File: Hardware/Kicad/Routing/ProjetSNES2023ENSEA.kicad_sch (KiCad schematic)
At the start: 43 parts, among them J1 Conn_01x07_Socket, Q1 2N7002, Q2 2N7002, Q3 2N7002, SW1 SW_Push, U1 NRF24L01, U2 AMS1117-3.3, U3 STM32L412KBTx, Y1 16 MHz

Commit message: Updated Schematic & PCB
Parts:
- renumbered D2 to D1, D1 to D2, R9 to R10, R10 to R9
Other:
- note added: "LEDs System"
- note added: "Mounting Holes"
- note added: "NES Port"
- note removed: "Mounting holes"
- note removed: "Port NES"
- note removed: "System LEDs"
- moved on the sheet: D1, D2, D3, H1, H2, H3, H4, Q1, Q2, Q3, R10, R11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

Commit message: Updated Schematic & PCB (New netclasses / Antenna still need to be connected)
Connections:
- net GND: no longer Antenna_nRF1.2 (GND), C3.2, J1.7 (Pin_7), R1.2, U1.14 (VSS), U1.17 (VSS), U1.20 (VSS), U1.8 (VSS)
- new net GND1: C3.2, R1.2, U1.14 (VSS), U1.17 (VSS), U1.20 (VSS), U1.8 (VSS)
- new net GND2: Antenna_nRF1.2 (GND)
- new net GND3: J1.7 (Pin_7)
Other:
- title: Wireless SNES Receptor (made by Esteban HUBERT) -> Wireless SNES Receiver
- moved on the sheet: C6, C7, C9, R1

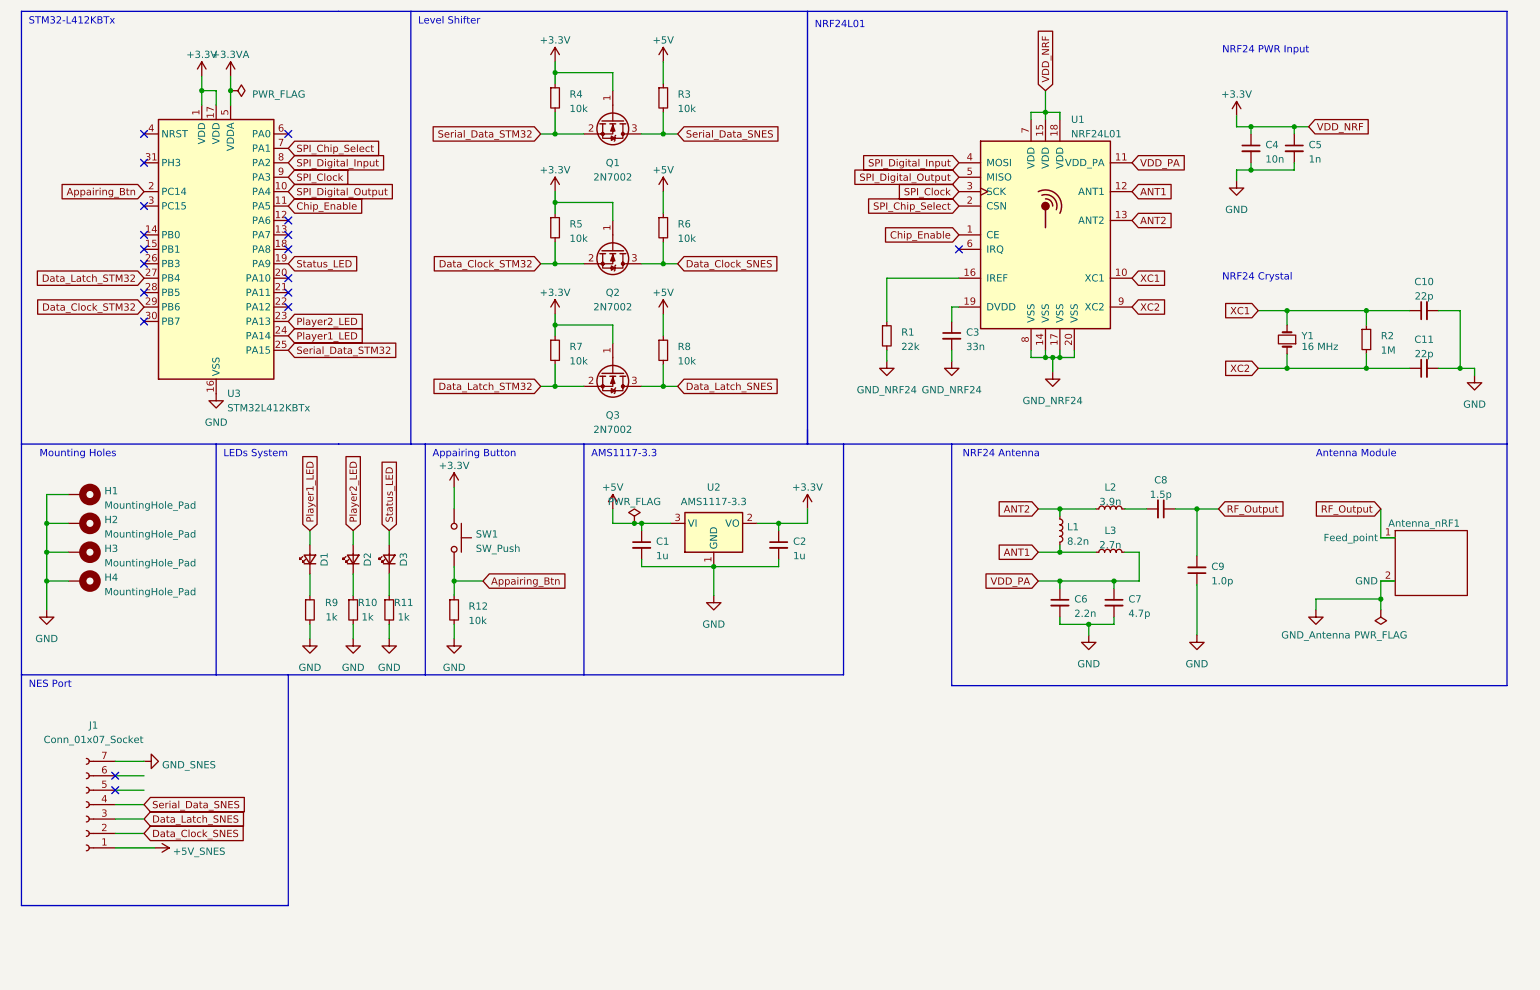
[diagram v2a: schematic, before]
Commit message: Updated Schematic & PCB (Netclass, Power Flag, Library, Antenna)
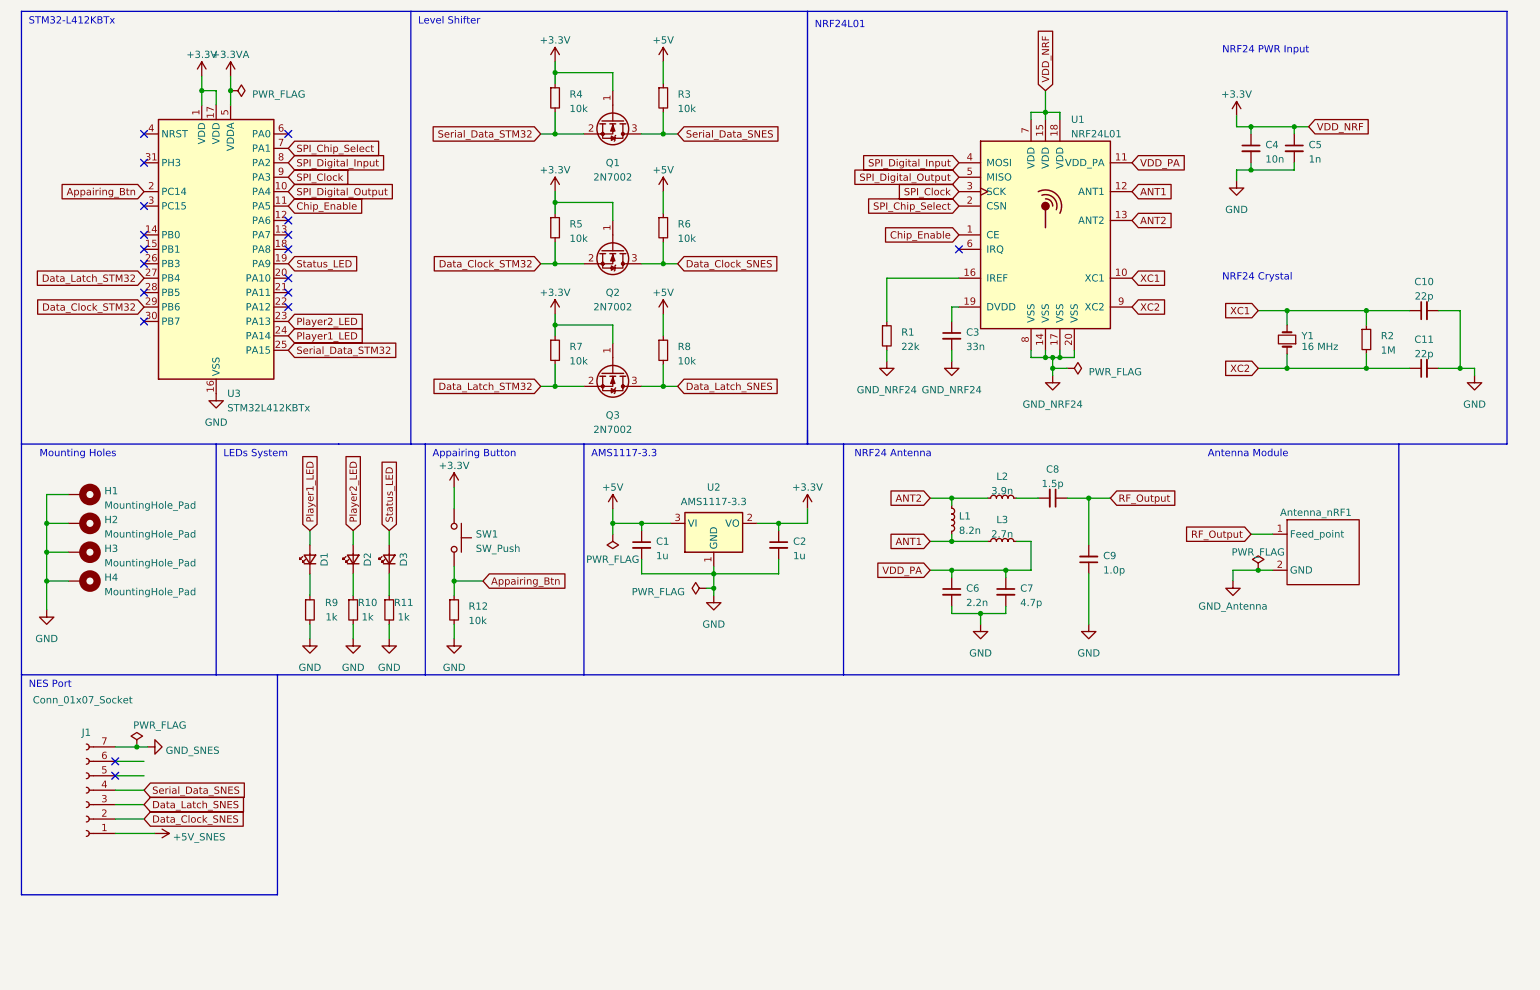
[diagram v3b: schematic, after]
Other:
- moved on the sheet: Antenna_nRF1, C6, C7, C8, C9, J1, L1, L2, L3
